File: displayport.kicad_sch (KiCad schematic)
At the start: 56 parts, among them J11 Connector_Displayport_Source, U1 MIMX8MM6DVTLZAA, U36 LP5912-1.2DRV, U37 SN65DSI86, U38 TPD4E02B04, U39 TPD4E02B04, U40 TPD4E02B04, X1 26Mhz

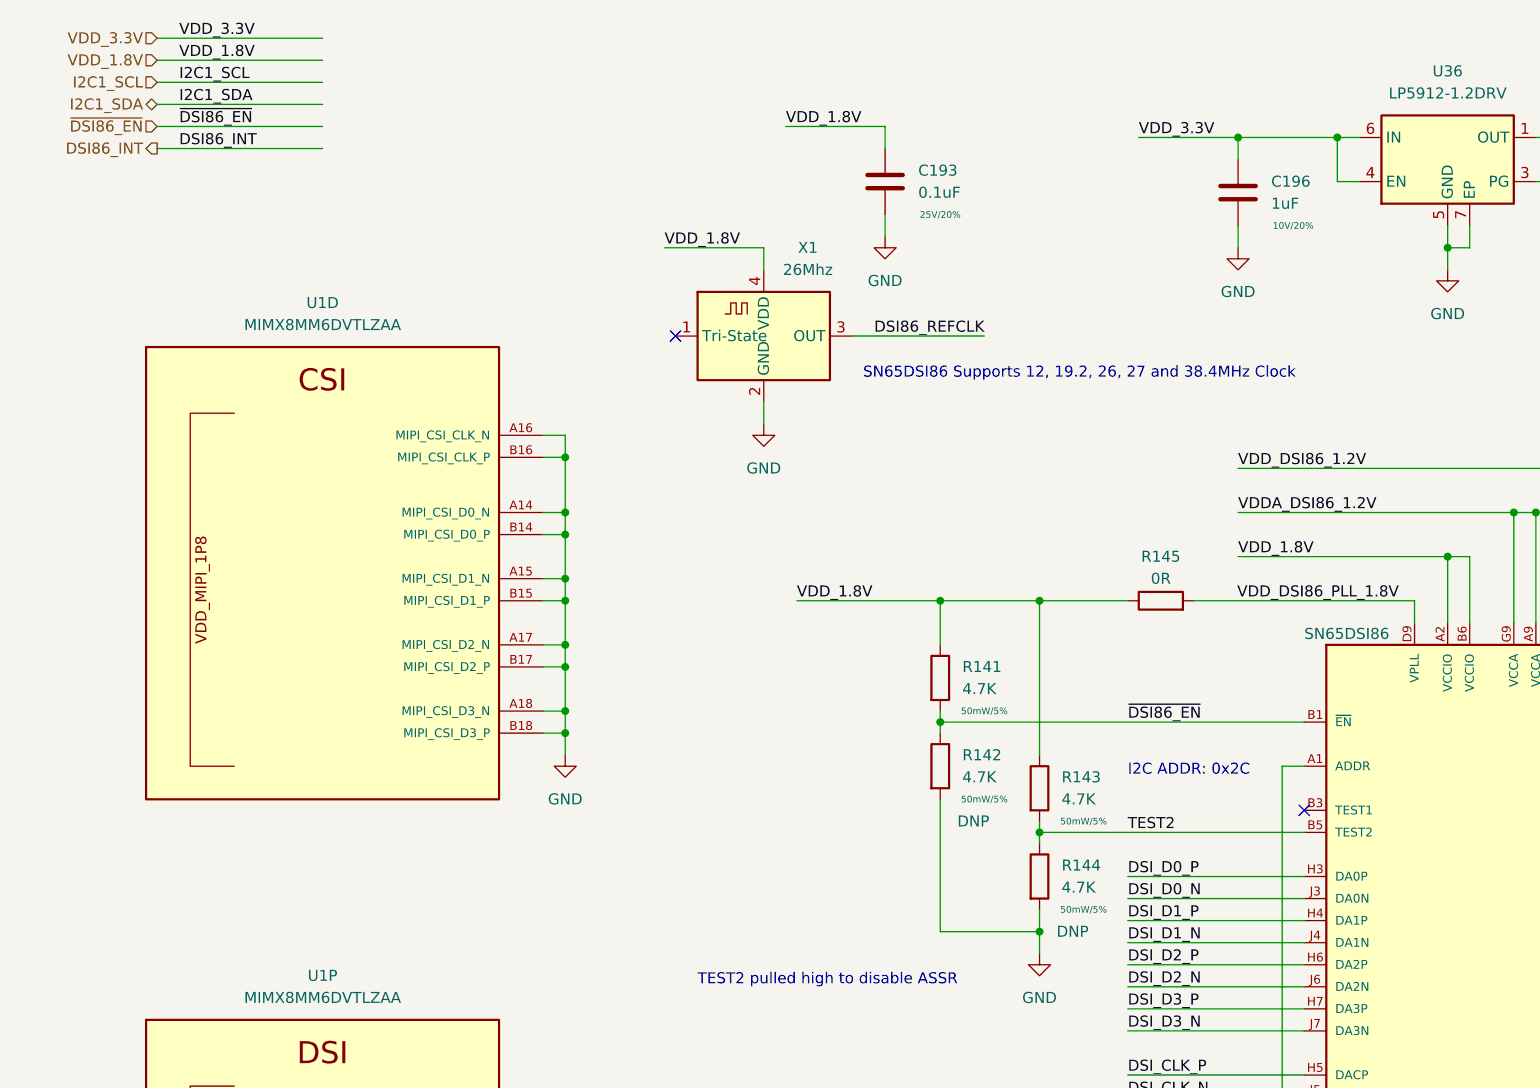
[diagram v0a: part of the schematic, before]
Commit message: dsi86: en is active high
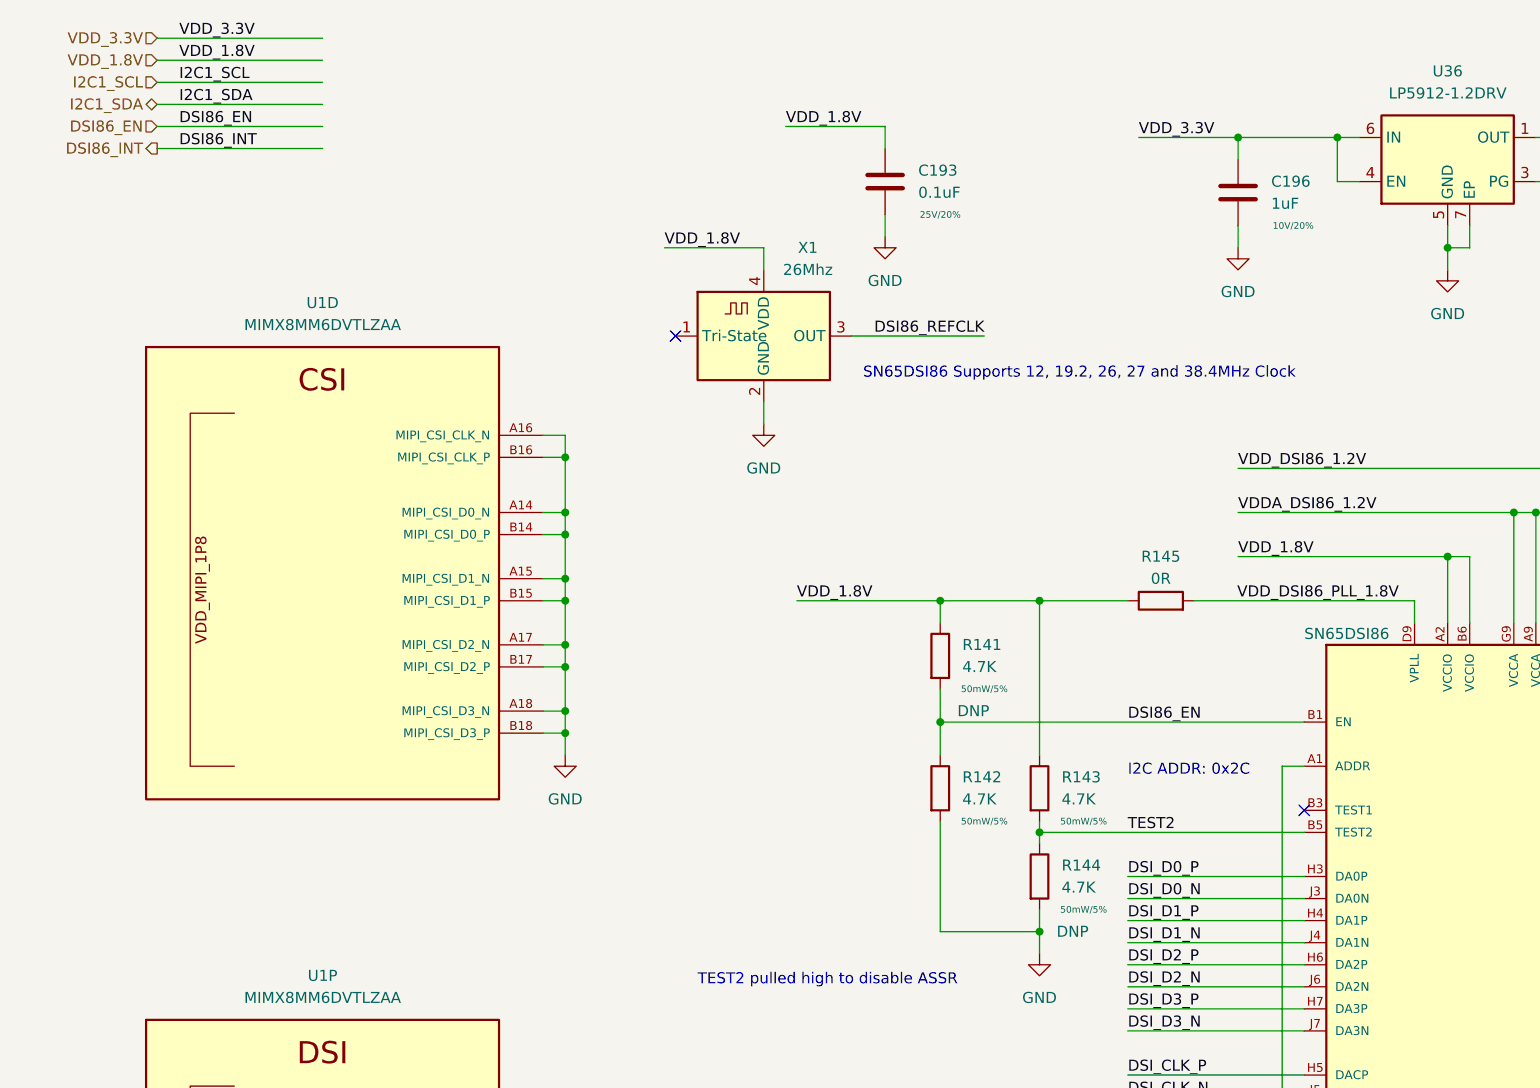
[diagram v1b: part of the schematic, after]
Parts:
- R141: DNP (none) -> DNP
- R142: DNP DNP -> (none)
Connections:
- net ~{DSI86_EN} renamed DSI86_EN
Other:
- moved on the sheet: R141, R142
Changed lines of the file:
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@@
-    (stroke (width 0) (type default) (color 0 0 0 0))
-  )
-  (wire (pts (xy 116.84 106.68) (xy 116.84 121.92))
     (stroke (width 0) (type default) (color 0 0 0 0))
   )
@@
     (stroke (width 0) (type default) (color 0 0 0 0))
   )
-  (wire (pts (xy 116.84 99.06) (xy 116.84 97.79))
+  (wire (pts (xy 116.84 97.79) (xy 116.84 101.6))
     (stroke (width 0) (type default) (color 0 0 0 0))
   )
@@
     (stroke (width 0) (type default) (color 0 0 0 0))
   )
-  (wire (pts (xy 116.84 96.52) (xy 116.84 97.79))
-    (stroke (width 0) (type default) (color 0 0 0 0))
-  )
   (wire (pts (xy 215.9 30.48) (xy 218.44 30.48))
     (stroke (width 0) (type default) (color 0 0 0 0))
@@
     (stroke (width 0) (type default) (color 0 0 0 0))
   )
+  (wire (pts (xy 116.84 93.98) (xy 116.84 97.79))
+    (stroke (width 0) (type default) (color 0 0 0 0))
+  )
   (wire (pts (xy 203.2 86.36) (xy 203.2 68.58))
     (stroke (width 0) (type default) (color 0 0 0 0))
@@
     (stroke (width 0) (type default) (color 0 0 0 0))
   )
-  (wire (pts (xy 116.84 83.82) (xy 116.84 88.9))
+  (wire (pts (xy 116.84 83.82) (xy 116.84 86.36))
     (stroke (width 0) (type default) (color 0 0 0 0))
   )
@@
   )
   (wire (pts (xy 367.03 129.54) (xy 369.57 129.54))
+    (stroke (width 0) (type default) (color 0 0 0 0))
+  )
+  (wire (pts (xy 116.84 109.22) (xy 116.84 121.92))
     (stroke (width 0) (type default) (color 0 0 0 0))
   )
@@
     (effects (font (size 1.27 1.27)) (justify left bottom))
   )
-  (label "~{DSI86_EN}" (at 29.21 29.21 0)
+  (label "DSI86_EN" (at 29.21 29.21 0)
     (effects (font (size 1.27 1.27)) (justify left bottom))
   )
@@
     (effects (font (size 1.27 1.27)) (justify left bottom))
   )
-  (label "~{DSI86_EN}" (at 138.43 97.79 0)
+  (label "DSI86_EN" (at 138.43 97.79 0)
     (effects (font (size 1.27 1.27)) (justify left bottom))
   )
@@
     (effects (font (size 1.27 1.27)) (justify right))
   )
-  (hierarchical_label "~{DSI86_EN}" (shape input) (at 26.67 29.21 180)
+  (hierarchical_label "DSI86_EN" (shape input) (at 26.67 29.21 180)
     (effects (font (size 1.27 1.27)) (justify right))
   )
@@
     (pin "1")
   )
-  (symbol (lib_id "Device:R") (at 116.84 102.87 0) (unit 1)
+  (symbol (lib_id "Device:R") (at 116.84 105.41 0) (unit 1)
     (in_bom no) (on_board yes)
-    (property "Reference" "R142" (id 0) (at 119.38 101.5999 0)
-      (effects (font (size 1.27 1.27)) (justify left))
-    )
-    (property "Value" "4.7K" (id 1) (at 119.38 104.1399 0)
-      (effects (font (size 1.27 1.27)) (justify left))
-    )
-    (property "Footprint" "qsbc:R_0402_1005Metric" (id 2) (at 115.062 102.87 90)
-      (effects (font (size 1.27 1.27)) hide)
-    )
-    (property "Datasheet" "~" (id 3) (at 116.84 102.87 0)
-      (effects (font (size 1.27 1.27)) hide)
-    )
-    (property "Rating" "50mW/5%" (id 4) (at 121.92 106.68 0)
-      (effects (font (size 0.762 0.762)))
-    )
-    (property "DNP" "DNP" (id 5) (at 120.65 109.22 0))
-    (property "MPN" "RC0402JR-074K7L" (id 6) (at 116.84 102.87 0)
+    (property "Reference" "R142" (id 0) (at 119.38 104.1399 0)
+      (effects (font (size 1.27 1.27)) (justify left))
+    )
+    (property "Value" "4.7K" (id 1) (at 119.38 106.6799 0)
+      (effects (font (size 1.27 1.27)) (justify left))
+    )
+    (property "Footprint" "qsbc:R_0402_1005Metric" (id 2) (at 115.062 105.41 90)
+      (effects (font (size 1.27 1.27)) hide)
+    )
+    (property "Datasheet" "~" (id 3) (at 116.84 105.41 0)
+      (effects (font (size 1.27 1.27)) hide)
+    )
+    (property "Rating" "50mW/5%" (id 4) (at 121.92 109.22 0)
+      (effects (font (size 0.762 0.762)))
+    )
+    (property "MPN" "RC0402JR-074K7L" (id 6) (at 116.84 105.41 0)
       (effects (font (size 1.27 1.27)) hide)
     )
@@
     (pin "2")
   )
-  (symbol (lib_id "Device:R") (at 116.84 92.71 0) (unit 1)
-    (in_bom yes) (on_board yes)
-    (property "Reference" "R141" (id 0) (at 119.38 91.4399 0)
-      (effects (font (size 1.27 1.27)) (justify left))
-    )
-    (property "Value" "4.7K" (id 1) (at 119.38 93.9799 0)
-      (effects (font (size 1.27 1.27)) (justify left))
-    )
-    (property "Footprint" "qsbc:R_0402_1005Metric" (id 2) (at 115.062 92.71 90)
-      (effects (font (size 1.27 1.27)) hide)
-    )
-    (property "Datasheet" "~" (id 3) (at 116.84 92.71 0)
-      (effects (font (size 1.27 1.27)) hide)
-    )
-    (property "Rating" "50mW/5%" (id 4) (at 121.92 96.52 0)
-      (effects (font (size 0.762 0.762)))
-    )
-    (property "MPN" "RC0402JR-074K7L" (id 5) (at 116.84 92.71 0)
-      (effects (font (size 1.27 1.27)) hide)
-    )
-    (pin "1")
-    (pin "2")
+  (symbol (lib_id "Device:R") (at 116.84 90.17 0) (unit 1)
+    (in_bom yes) (on_board yes)
+    (property "Reference" "R141" (id 0) (at 119.38 88.8999 0)
+      (effects (font (size 1.27 1.27)) (justify left))
+    )
+    (property "Value" "4.7K" (id 1) (at 119.38 91.4399 0)
+      (effects (font (size 1.27 1.27)) (justify left))
+    )
+    (property "Footprint" "qsbc:R_0402_1005Metric" (id 2) (at 115.062 90.17 90)
+      (effects (font (size 1.27 1.27)) hide)
+    )
+    (property "Datasheet" "~" (id 3) (at 116.84 90.17 0)
+      (effects (font (size 1.27 1.27)) hide)
+    )
+    (property "Rating" "50mW/5%" (id 4) (at 121.92 93.98 0)
+      (effects (font (size 0.762 0.762)))
+    )
+    (property "MPN" "RC0402JR-074K7L" (id 5) (at 116.84 90.17 0)
+      (effects (font (size 1.27 1.27)) hide)
+    )
+    (property "DNP" "DNP" (id 6) (at 120.65 96.52 0))
+    (pin "1")
+    (pin "2")
